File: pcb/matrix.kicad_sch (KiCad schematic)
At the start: 136 parts

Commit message: Update schematic
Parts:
- removed MX68, MX72: 1u, MX_Only:MXOnly-1U-NoLED, symbol Switch:SW_SPST
- removed MX69, MX71, MX73: 1.5u, MX_Only:MXOnly-1.5U-NoLED, symbol Switch:SW_SPST
- added D59, D61: 1N4148, Diode_SMD:D_SOD-123, symbol Device:D
- added MX62: 2.25, MX_Only:MXOnly-6.25U-ReversedStabilizers-NoLED, symbol Switch:SW_SPST
- added MX63: 2.75u, MX_Only:MXOnly-7U-ReversedStabilizers-NoLED, symbol Switch:SW_SPST
- added MX66: 2.75u, MX_Only:MXOnly-6.25U-ReversedStabilizers-NoLED, symbol Switch:SW_SPST
- MX64: renamed from MX62; value 6.25u -> 1.25u
- MX65: renamed from MX70; value 7u -> 1.25u
- MX67: value 1.5u -> 2.25u; footprint MX_Only:MXOnly-1.5U-NoLED -> MX_Only:MXOnly-7U-ReversedStabilizers-NoLED
- renumbered D59 to D60, D60 to D62, D61 to D63, D62 to D64, D63 to D65, MX63 to MX68, MX64 to MX69, MX65 to MX70, MX66 to MX71
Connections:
- net COL0: no longer MX67.2 (B)
- net COL4: now also MX62.2 (B), MX63.2 (B)
- net COL8: now also MX67.2 (B), MX66.2 (B)
- net ROW4: now also D59.1 (K), D61.1 (K)
- net at D56.2 (A), MX59.1 (A): no longer MX67.1 (A)
- new net: D61.2 (A), MX66.1 (A), MX67.1 (A)
- new net: D59.2 (A), MX62.1 (A), MX63.1 (A)

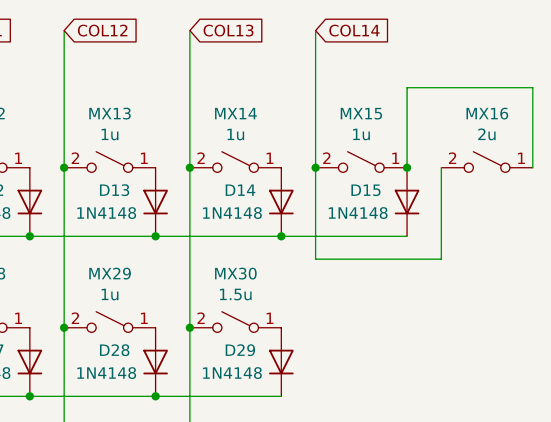
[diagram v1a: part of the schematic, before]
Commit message: Convert remaining top row to hotswap
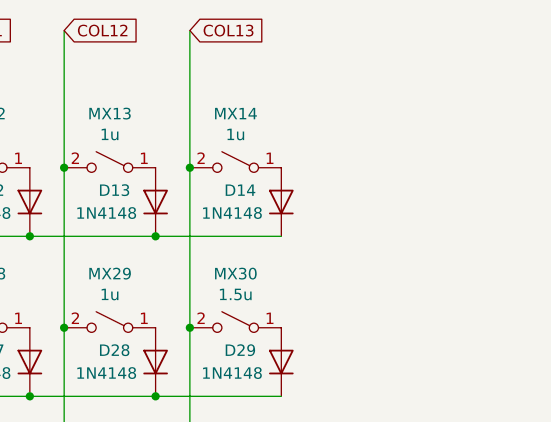
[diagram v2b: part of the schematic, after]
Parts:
- removed D15: 1N4148, Diode_SMD:D_SOD-123, symbol Device:D
- removed MX15: 1u, MX_Only:MXOnly-1U-NoLED, symbol Switch:SW_SPST
- removed MX16: 2u, MX_Only:MXOnly-2U-NoLED, symbol Switch:SW_SPST
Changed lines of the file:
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@@
   (junction (at 223.52 92.71) (diameter 0) (color 0 0 0 0)
   )
-  (junction (at 251.46 39.37) (diameter 0) (color 0 0 0 0)
-  )
   (junction (at 45.72 39.37) (diameter 0) (color 0 0 0 0)
   )
@@
   (junction (at 69.85 64.77) (diameter 0) (color 0 0 0 0)
   )
-  (junction (at 237.49 46.99) (diameter 0) (color 0 0 0 0)
-  )
   (junction (at 195.58 100.33) (diameter 0) (color 0 0 0 0)
   )
-  (junction (at 241.3 39.37) (diameter 0) (color 0 0 0 0)
-  )
   (wire (pts (xy 223.52 46.99) (xy 209.55 46.99))
     (stroke (width 0) (type default) (color 0 0 0 0))
   )
-  (wire (pts (xy 265.43 39.37) (xy 265.43 30.48))
-    (stroke (width 0) (type default) (color 0 0 0 0))
-  )
   (wire (pts (xy 73.66 39.37) (xy 73.66 57.15))
     (stroke (width 0) (type default) (color 0 0 0 0))
@@
     (stroke (width 0) (type default) (color 0 0 0 0))
   )
-  (wire (pts (xy 265.43 30.48) (xy 251.46 30.48))
-    (stroke (width 0) (type default) (color 0 0 0 0))
-  )
   (wire (pts (xy 171.45 57.15) (xy 171.45 74.93))
     (stroke (width 0) (type default) (color 0 0 0 0))
@@
     (stroke (width 0) (type default) (color 0 0 0 0))
   )
-  (wire (pts (xy 255.27 49.53) (xy 255.27 39.37))
-    (stroke (width 0) (type default) (color 0 0 0 0))
-  )
   (wire (pts (xy 83.82 82.55) (xy 69.85 82.55))
     (stroke (width 0) (type default) (color 0 0 0 0))
@@
     (stroke (width 0) (type default) (color 0 0 0 0))
   )
-  (wire (pts (xy 241.3 49.53) (xy 255.27 49.53))
-    (stroke (width 0) (type default) (color 0 0 0 0))
-  )
   (wire (pts (xy 129.54 24.13) (xy 129.54 39.37))
     (stroke (width 0) (type default) (color 0 0 0 0))
@@
     (stroke (width 0) (type default) (color 0 0 0 0))
   )
-  (wire (pts (xy 241.3 39.37) (xy 241.3 49.53))
-    (stroke (width 0) (type default) (color 0 0 0 0))
-  )
   (wire (pts (xy 181.61 82.55) (xy 167.64 82.55))
     (stroke (width 0) (type default) (color 0 0 0 0))
@@
     (stroke (width 0) (type default) (color 0 0 0 0))
   )
-  (wire (pts (xy 241.3 24.13) (xy 241.3 39.37))
-    (stroke (width 0) (type default) (color 0 0 0 0))
-  )
   (wire (pts (xy 115.57 92.71) (xy 115.57 74.93))
     (stroke (width 0) (type default) (color 0 0 0 0))
@@
     (stroke (width 0) (type default) (color 0 0 0 0))
   )
-  (wire (pts (xy 251.46 30.48) (xy 251.46 39.37))
-    (stroke (width 0) (type default) (color 0 0 0 0))
-  )
   (wire (pts (xy 171.45 24.13) (xy 171.45 39.37))
     (stroke (width 0) (type default) (color 0 0 0 0))
@@
   )
   (wire (pts (xy 213.36 102.87) (xy 213.36 110.49))
-    (stroke (width 0) (type default) (color 0 0 0 0))
-  )
-  (wire (pts (xy 251.46 46.99) (xy 237.49 46.99))
     (stroke (width 0) (type default) (color 0 0 0 0))
   )
@@
     )
   )
-  (global_label "COL14" (shape input) (at 241.3 24.13 0) (fields_autoplaced)
-    (effects (font (size 1.27 1.27)) (justify left))
-    (property "Intersheet References" "${INTERSHEET_REFS}" (id 0) (at 0 0 0)
-      (effects (font (size 1.27 1.27)) hide)
-    )
-  )
   (global_label "COL13" (shape input) (at 227.33 24.13 0) (fields_autoplaced)
     (effects (font (size 1.27 1.27)) (justify left))
@@
     (pin "2")
   )
-  (symbol (lib_id "Switch:SW_SPST") (at 260.35 39.37 0) (mirror y) (unit 1)
-    (in_bom yes) (on_board yes)
-    (property "Reference" "MX16" (id 0) (at 260.35 33.401 0))
-    (property "Value" "2u" (id 1) (at 260.35 35.7124 0))
-    (property "Footprint" "MX_Only:MXOnly-2U-NoLED" (id 2) (at 260.35 39.37 0)
-      (effects (font (size 1.27 1.27)) hide)
-    )
-    (property "Datasheet" "~" (id 3) (at 260.35 39.37 0)
-      (effects (font (size 1.27 1.27)) hide)
-    )
-    (pin "1")
-    (pin "2")
-  )
   (symbol (lib_id "Switch:SW_SPST") (at 50.8 74.93 0) (mirror y) (unit 1)
     (in_bom yes) (on_board yes)
@@
       (effects (font (size 1.27 1.27)) hide)
     )
-    (pin "1")
-    (pin "2")
-  )
-  (symbol (lib_id "Device:D") (at 251.46 43.18 90) (unit 1)
-    (in_bom yes) (on_board yes)
-    (property "Reference" "D15" (id 0) (at 245.11 41.91 90)
-      (effects (font (size 1.27 1.27)) (justify right))
-    )
-    (property "Value" "1N4148" (id 1) (at 242.57 44.45 90)
-      (effects (font (size 1.27 1.27)) (justify right))
-    )
-    (property "Footprint" "Diode_SMD:D_SOD-123" (id 2) (at 251.46 43.18 0)
-      (effects (font (size 1.27 1.27)) hide)
-    )
-    (property "Datasheet" "~" (id 3) (at 251.46 43.18 0)
-      (effects (font (size 1.27 1.27)) hide)
-    )
-    (property "LCSC Part #" "C81598" (id 4) (at 251.46 43.18 0)
-      (effects (font (size 1.27 1.27)) hide)
-    )
-    (pin "1")
-    (pin "2")
-  )
-  (symbol (lib_id "Switch:SW_SPST") (at 246.38 39.37 0) (mirror y) (unit 1)
-    (in_bom yes) (on_board yes)
-    (property "Reference" "MX15" (id 0) (at 246.38 33.401 0))
-    (property "Value" "1u" (id 1) (at 246.38 35.7124 0))
-    (property "Footprint" "MX_Only:MXOnly-1U-NoLED" (id 2) (at 246.38 39.37 0)
-      (effects (font (size 1.27 1.27)) hide)
-    )
-    (property "Datasheet" "~" (id 3) (at 246.38 39.37 0)
-      (effects (font (size 1.27 1.27)) hide)
-    )
